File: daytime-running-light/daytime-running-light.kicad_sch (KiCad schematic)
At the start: 47 parts, among them J1 Conn_01x01_Socket, J2 Conn_01x01_Socket, J3 Conn_01x01_Socket, J4 Conn_01x02_Socket, Q1 2N3904, Q2 2N3904, Q3 IRFZ44N, Q4 IRF9321, SW1 SW_SPST, SW2 SW_SPST, U1 L7812, U2 4069, U3 4001

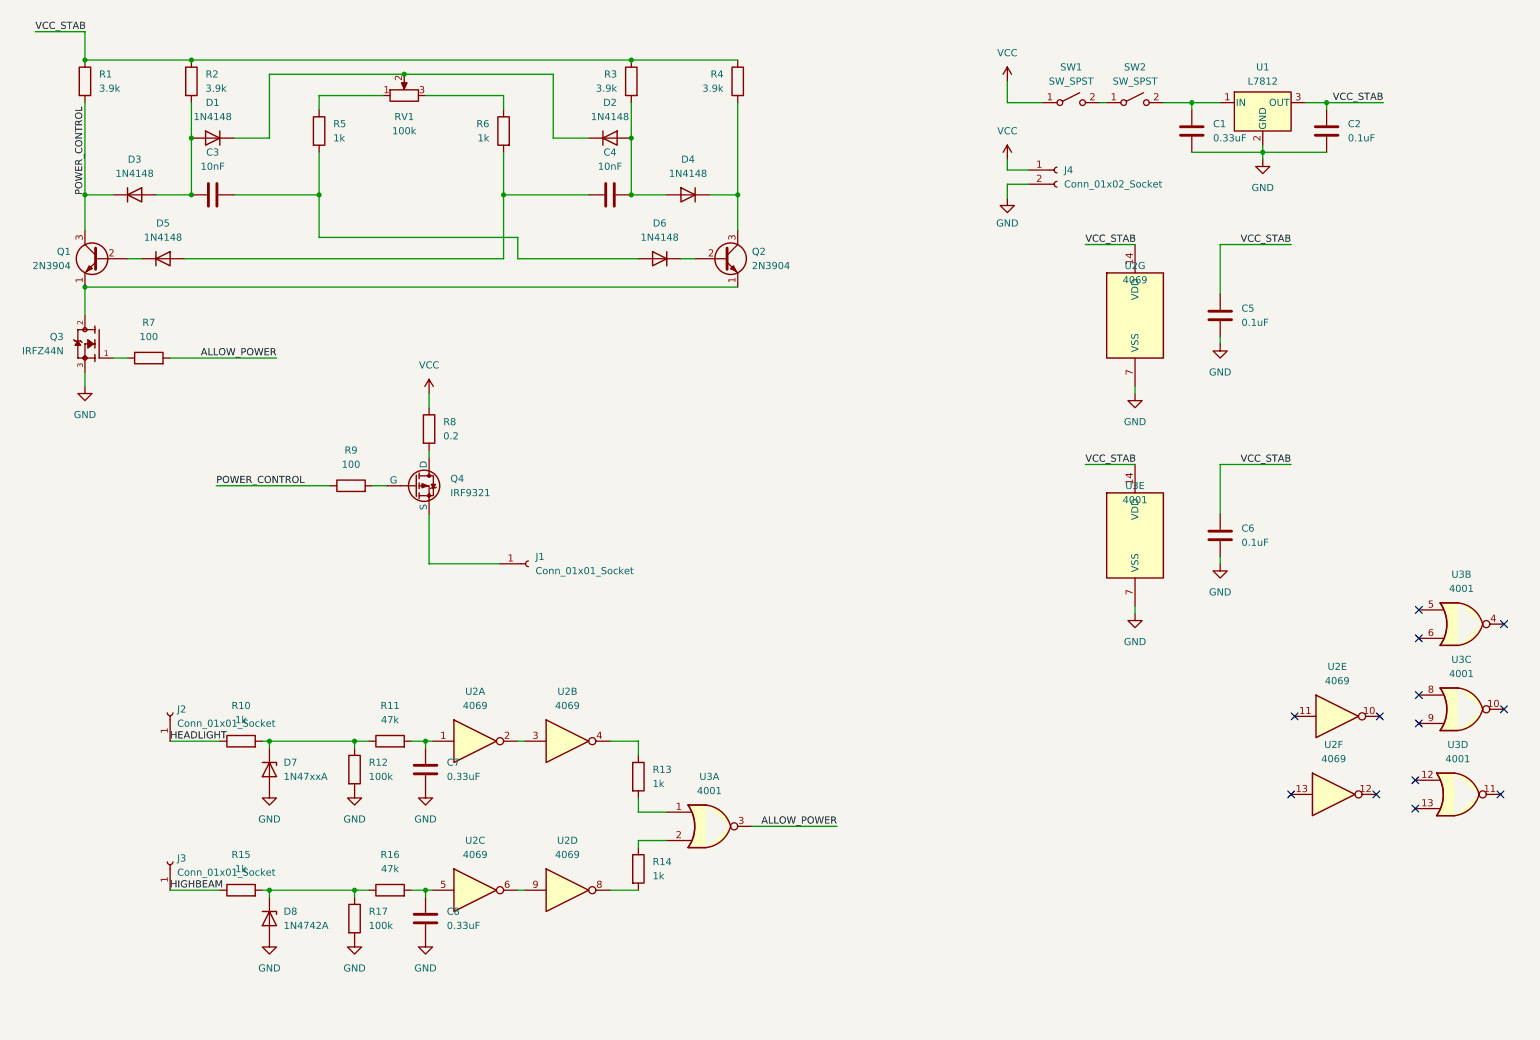
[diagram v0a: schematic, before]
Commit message: [drl] Change daytime running light to use TLC555 timer.
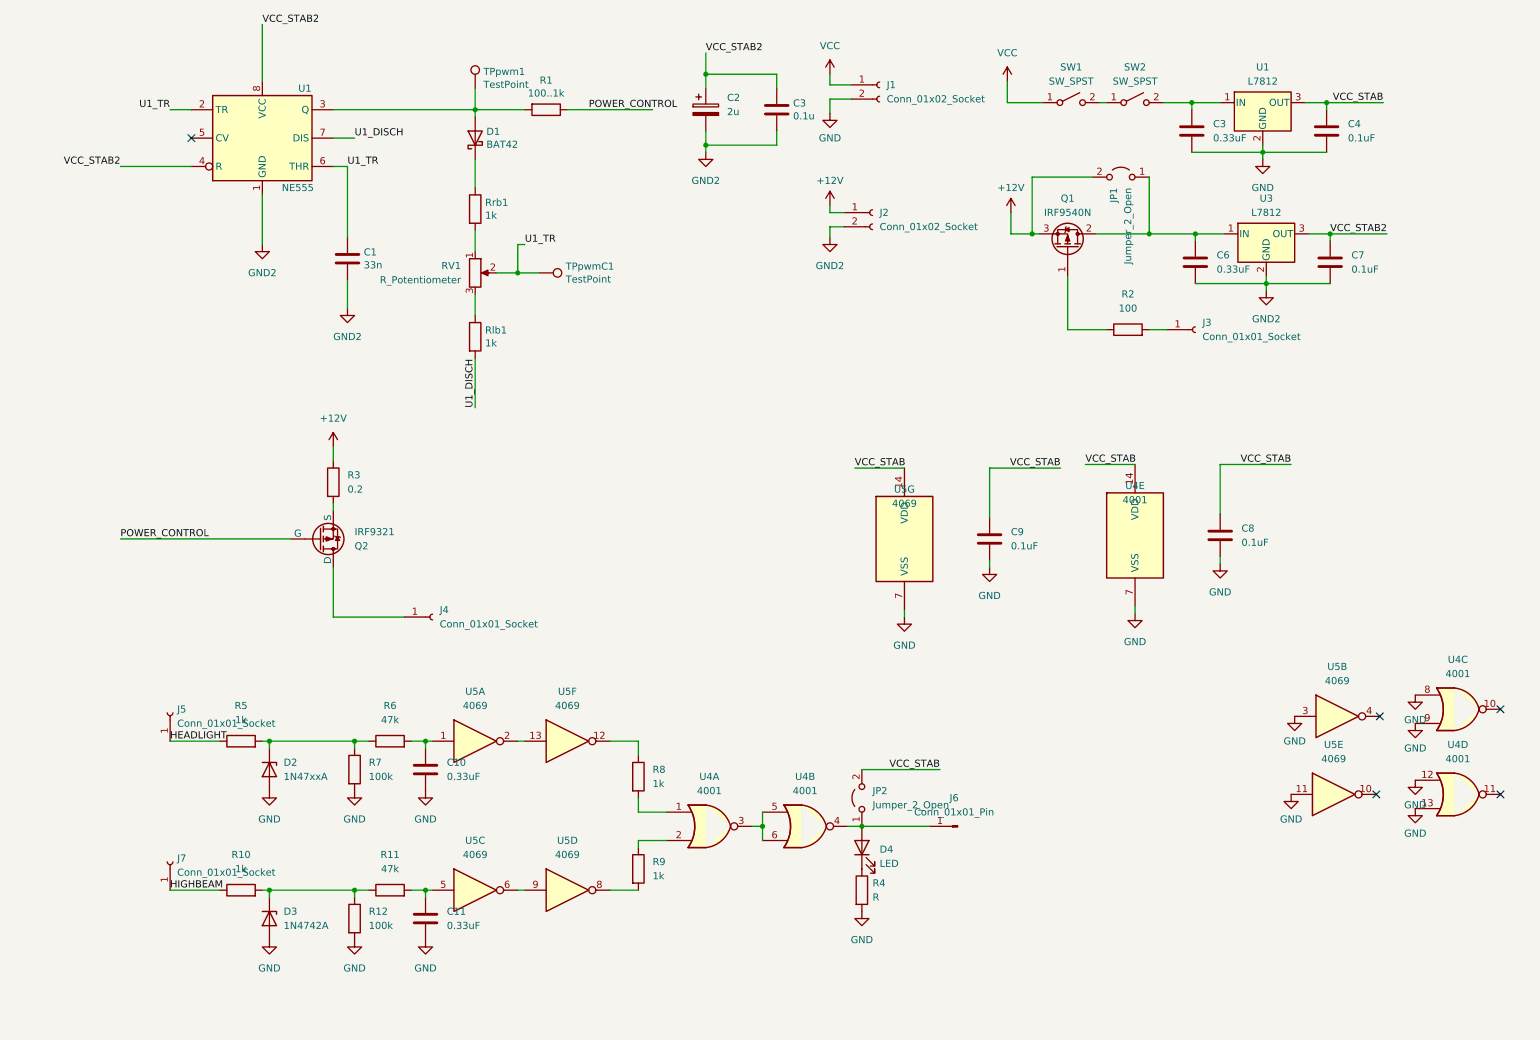
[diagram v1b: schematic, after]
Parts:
- removed C4: 10nF, Capacitor_THT:C_Disc_D6.0mm_W2.5mm_P5.00mm, symbol Device:C
- removed D1, D2, D3, D4, D5, D6: 1N4148, Diode_THT:D_DO-35_SOD27_P7.62mm_Horizontal, symbol Diode:1N4148
- removed Q1, Q2: 2N3904, Package_TO_SOT_THT:TO-92_Inline, symbol Transistor_BJT:2N3904
- removed Q3: IRFZ44N, Package_TO_SOT_THT:TO-220-3_Vertical, symbol IRFZ44N:IRFZ44N
- removed R2, R3: 3.9k, Resistor_THT:R_Axial_DIN0207_L6.3mm_D2.5mm_P7.62mm_Horizontal, symbol Device:R
- removed R5, R6: 1k, Resistor_THT:R_Axial_DIN0207_L6.3mm_D2.5mm_P2.54mm_Vertical, symbol Device:R
- removed R9: 100, Resistor_THT:R_Axial_DIN0207_L6.3mm_D2.5mm_P2.54mm_Vertical, symbol Device:R
- added C1: 33n, Capacitor_THT:C_Disc_D6.0mm_W2.5mm_P5.00mm, symbol Device:C
- added C2: 2u, Capacitor_THT:CP_Radial_D6.3mm_P2.50mm, symbol Device:C_Polarized
- added C6: 0.33uF, Capacitor_THT:C_Disc_D6.0mm_W2.5mm_P5.00mm, symbol Device:C
- added C7: 0.1uF, Capacitor_THT:C_Disc_D6.0mm_W2.5mm_P5.00mm, symbol Device:C
- added D1: BAT42, Diode_THT:D_DO-35_SOD27_P7.62mm_Horizontal, symbol Diode:BAT42
- added D4: LED, Connector_Wire:SolderWire-0.5sqmm_1x02_P4.6mm_D0.9mm_OD2.1mm, symbol Device:LED
- added J2: Conn_01x02_Socket, Connector_Wire:SolderWire-2.5sqmm_1x02_P8.8mm_D2.4mm_OD4.4mm, symbol Connector:Conn_01x02_Socket
- added J3: Conn_01x01_Socket, Connector_Wire:SolderWire-1.5sqmm_1x01_D1.7mm_OD3mm, symbol Connector:Conn_01x01_Socket
- added J6: Conn_01x01_Pin, Connector_Wire:SolderWire-1.5sqmm_1x01_D1.7mm_OD3mm, symbol Connector:Conn_01x01_Pin
- added JP1, JP2: Jumper_2_Open, Connector_Wire:SolderWire-0.75sqmm_1x02_P4.8mm_D1.25mm_OD2.3mm, symbol Jumper:Jumper_2_Open
- added Q1: IRF9540N, Package_TO_SOT_THT:TO-220-3_Vertical, symbol Transistor_FET:IRF9540N
- added Rlb1, Rrb1: 1k, Resistor_THT:R_Axial_DIN0207_L6.3mm_D2.5mm_P2.54mm_Vertical, symbol Device:R
- added TPpwm1, TPpwmC1: TestPoint, TestPoint:TestPoint_Pad_4.0x4.0mm, symbol Connector:TestPoint
- added U1: NE555, Package_DIP:DIP-8_W7.62mm, symbol smoke-machine-rescue:NE555-Timer
- added U3: L7812, Package_TO_SOT_THT:TO-220-3_Vertical, symbol Regulator_Linear:L7812
- C3: value 10nF -> 0.1u
- J1: renamed from J4; footprint Connector_Wire:SolderWire-2.5sqmm_1x02_P8.8mm_D2.4mm_OD4.4mm_Relief -> Connector_Wire:SolderWire-2.5sqmm_1x02_P8.8mm_D2.4mm_OD4.4mm
- J4: renamed from J1; footprint Connector_Wire:SolderWire-2.5sqmm_1x01_D2.4mm_OD3.6mm_Relief -> Connector_Wire:SolderWire-2.5sqmm_1x01_D2.4mm_OD3.6mm
- J5: renamed from J2; footprint Connector_Wire:SolderWire-1.5sqmm_1x01_D1.7mm_OD3mm_Relief -> Connector_Wire:SolderWire-1.5sqmm_1x01_D1.7mm_OD3mm
- J7: renamed from J3; footprint Connector_Wire:SolderWire-1.5sqmm_1x01_D1.7mm_OD3mm_Relief -> Connector_Wire:SolderWire-1.5sqmm_1x01_D1.7mm_OD3mm
- R1: value 3.9k -> 100..1k
- R3: renamed from R8; footprint Connector_Wire:SolderWire-1sqmm_1x02_P5.4mm_D1.4mm_OD2.7mm_Relief -> Connector_Wire:SolderWire-1sqmm_1x02_P5.4mm_D1.4mm_OD2.7mm
- R4: value 3.9k -> R
- RV1: value 100k -> R_Potentiometer; footprint Connector_Wire:SolderWire-1.5sqmm_1x03_P6mm_D1.7mm_OD3mm_Relief -> Connector_Wire:SolderWire-0.1sqmm_1x03_P3.6mm_D0.4mm_OD1mm_Relief
- SW1, SW2: footprint Connector_Wire:SolderWire-1.5sqmm_1x02_P6mm_D1.7mm_OD3mm_Relief -> Connector_Wire:SolderWire-2.5sqmm_1x02_P8.8mm_D2.4mm_OD4.4mm
- U1: footprint Package_TO_SOT_THT:TO-220-3_Horizontal_TabUp -> Package_TO_SOT_THT:TO-220-3_Vertical
- renumbered C7 to C10, C8 to C11, C1 to C3, C2 to C4, C6 to C8, C5 to C9, D7 to D2, D8 to D3, Q4 to Q2, R15 to R10, R16 to R11, R17 to R12, R7 to R2, R10 to R5, R11 to R6, R12 to R7, R13 to R8, R14 to R9, U3 to U4, U2 to U5
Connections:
- net GND: now also R4.2, U4.12, U4.13, U4.8, U4.9, U5.11, U5.3
- net POWER_CONTROL: now also Q2.2 (G), R1.1; no longer R1.2
- net VCC: no longer R3.1
- net VCC_STAB: now also JP2.2 (B); no longer R1.1, R4.1
- net GND2: now reaches C3.2
- net GND2: now also C1.2, C2.2, C6.2, C7.2, J2.2 (Pin_2), U1.1 (GND), U3.2 (GND)
- net at RV1.1: now also Rrb1.2
- net at R3.2: now also Q2.3 (S); no longer Q2.1 (D)
- net VCC_STAB2: now reaches C3.1
- net VCC_STAB2: now also C2.1, C7.1, U1.4 (R), U1.8 (VCC), U3.3 (OUT)
- net U1_TR: now reaches RV1.2
- net U1_TR: now also C1.1, TPpwmC1.1, U1.2 (TR), U1.6 (THR)
- net at R2.1: now also Q1.1 (G)
- net at R8.1: now also U5.12; no longer U5.4
- net at RV1.3: now also Rlb1.1
- net at U5.2: now also U5.13; no longer U5.3
- net at J4.1 (Pin_1): now also Q2.1 (D); no longer Q2.3 (S)
- net ALLOW_POWER: no longer names the net of R2.2
- net ALLOW_POWER: now also J3.1 (Pin_1); no longer U4.3
- new net: D1.2 (A), R1.2, TPpwm1.1, U1.3 (Q)
- new net: C6.1, JP1.1 (A), Q1.2 (D), U3.1 (IN)
- new net: U4.3, U4.5, U4.6
- new net: D4.1 (K), R4.1
- new net: D1.1 (K), Rrb1.1
- new net: D4.2 (A), J6.1 (Pin_1), JP2.1 (A), U4.4
- new net +12V: J2.1 (Pin_1), JP1.2 (B), Q1.3 (S), R3.1
- new net U1_DISCH: Rlb1.2, U1.7 (DIS)
- no-connect marks 13 -> 5
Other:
- moved on the sheet: C9, J1, J4, Q2, R2, R3, U4B, U4C, U4D, U5G

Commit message: [drl] Change schematic and PCB
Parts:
- removed U1: NE555, Package_DIP:DIP-8_W7.62mm, symbol smoke-machine-rescue:NE555-Timer
- added D5: 1.5KExxA, Diode_THT:D_DO-201AE_P15.24mm_Horizontal, symbol Diode:1.5KExxA
- added D6: 1N4148, Diode_THT:D_DO-35_SOD27_P7.62mm_Horizontal, symbol Diode:1N4148
- added Q3, Q4: BC548, LIB:TO-92_HandSolder2, symbol Transistor_BJT:BC548
- added Q5: BC548, Package_TO_SOT_THT:TO-92_HandSolder, symbol Transistor_BJT:BC548
- added R13, R16: 100, Resistor_THT:R_Axial_DIN0207_L6.3mm_D2.5mm_P2.54mm_Vertical, symbol Device:R
- added R14, R15: 10k..100k, Resistor_THT:R_Axial_DIN0207_L6.3mm_D2.5mm_P2.54mm_Vertical, symbol Device:R
- added R17: 10k, Resistor_THT:R_Axial_DIN0207_L6.3mm_D2.5mm_P2.54mm_Vertical, symbol Device:R
- added U2: TLC555xP, Package_DIP:DIP-8_W7.62mm, symbol Timer:TLC555xP
- C2: value 2u -> 0.1u
- Q1, U3: footprint Package_TO_SOT_THT:TO-220-3_Vertical -> LIB:TO-220-3_Vertical-mod
- R1: value 100..1k -> 10k
- R2: value 100 -> 10k
- RV1: value R_Potentiometer -> 51k
- Rlb1: value 1k -> 51k
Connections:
- net +12V: now also R15.1
- net GND2: now also Q3.3 (E), Q4.3 (E), U2.1 (GND)
- net POWER_CONTROL: now also D1.2 (A), R1.2, TPpwm1.1, U2.3 (Q); no longer Q2.2 (G), R1.1
- net U1_DISCH: now also U2.7 (DIS)
- net U1_TR: now also U2.2 (TR), U2.6 (THR)
- net VCC_STAB2: now also R14.1, U2.8 (VCC)
- net ALLOW_POWER_ON: now reaches Q1.1 (G), R2.1
- net ALLOW_POWER_ON: now also Q3.2 (B)
- net at Q2.3 (S), R3.2: now also D5.1 (A1), Q5.1 (C), R17.2
- net at J4.1 (Pin_1), Q2.1 (D): now also D5.2 (A2)
- net at D4.2 (A), JP2.1 (A), U4.4: now also R13.1; no longer J6.1 (Pin_1)
- new net: D6.1 (K), Q5.2 (B), R16.2, R17.1
- new net: Q4.2 (B), R1.1
- new net: Q3.1 (C), R14.2, U2.4 (R)
- new net: J6.1 (Pin_1), R13.2
- new net: D6.2 (A), Q2.2 (G), Q5.3 (E)
- new net POWER_CONTROL_INV: Q4.1 (C), R15.2, R16.1
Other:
- moved on the sheet: C10, C11, C8, C9, D2, D3, D4, J3, J4, J5, J6, J7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

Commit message: [drl] Change schematic and PCB
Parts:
- added R18: R, Resistor_THT:R_Axial_DIN0207_L6.3mm_D2.5mm_P2.54mm_Vertical, symbol Device:R
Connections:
- net GND: now also R18.2; no longer R4.2
- net VCC_STAB: now also R4.2; no longer JP2.2 (B)
- net at D4.2 (A), R13.1, U4.4: now also JP2.2 (B); no longer JP2.1 (A)
- new net: JP2.1 (A), R18.1
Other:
- moved on the sheet: D4, JP2, R4
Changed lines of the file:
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@@
     (stroke (width 0) (type default))
   )
-  (wire (pts (xy 137.795 159.385) (xy 150.495 159.385))
+  (wire (pts (xy 137.795 154.305) (xy 150.495 154.305))
     (stroke (width 0) (type default))
   )
@@
     (stroke (width 0) (type default))
   )
-  (wire (pts (xy 137.795 159.385) (xy 137.795 160.655))
+  (wire (pts (xy 137.795 154.305) (xy 137.795 155.575))
     (stroke (width 0) (type default))
   )
@@
     (effects (font (size 1.27 1.27)) (justify right bottom))
   )
-  (label "VCC_STAB" (at 150.495 159.385 180) (fields_autoplaced)
+  (label "VCC_STAB" (at 150.495 154.305 180) (fields_autoplaced)
     (effects (font (size 1.27 1.27)) (justify right bottom))
   )
@@
     )
   )
+  (symbol (lib_id "Device:R") (at 137.795 184.785 0) (unit 1)
+    (in_bom yes) (on_board yes) (dnp no) (fields_autoplaced)
+    (property "Reference" "R18" (at 139.7 183.515 0)
+      (effects (font (size 1.27 1.27)) (justify left))
+    )
+    (property "Value" "R" (at 139.7 186.055 0)
+      (effects (font (size 1.27 1.27)) (justify left))
+    )
+    (property "Footprint" "Resistor_THT:R_Axial_DIN0207_L6.3mm_D2.5mm_P2.54mm_Vertical" (at 136.017 184.785 90)
+      (effects (font (size 1.27 1.27)) hide)
+    )
+    (property "Datasheet" "~" (at 137.795 184.785 0)
+      (effects (font (size 1.27 1.27)) hide)
+    )
+    (pin "1")
+    (pin "2")
+    (instances
+      (project "daytime-running-light"
+        (path "/f8c2c6dd-d5ef-40d1-be2c-9a93444b1d43"
+          (reference "R18") (unit 1)
+        )
+      )
+    )
+  )
   (symbol (lib_id "power:GND") (at 157.48 33.655 0) (unit 1)
     (in_bom yes) (on_board yes) (dnp no) (fields_autoplaced)
@@
     )
   )
+  (symbol (lib_id "power:GND") (at 137.795 188.595 0) (unit 1)
+    (in_bom yes) (on_board yes) (dnp no) (fields_autoplaced)
+    (property "Reference" "#PWR025" (at 137.795 194.945 0)
+      (effects (font (size 1.27 1.27)) hide)
+    )
+    (property "Value" "GND" (at 137.795 193.675 0)
+      (effects (font (size 1.27 1.27)))
+    )
+    (property "Footprint" "" (at 137.795 188.595 0)
+      (effects (font (size 1.27 1.27)) hide)
+    )
+    (property "Datasheet" "" (at 137.795 188.595 0)
+      (effects (font (size 1.27 1.27)) hide)
+    )
+    (pin "1")
+    (instances
+      (project "daytime-running-light"
+        (path "/f8c2c6dd-d5ef-40d1-be2c-9a93444b1d43"
+          (reference "#PWR025") (unit 1)
+        )
+      )
+    )
+  )
   (symbol (lib_id "power:GND") (at 31.75 164.465 0) (unit 1)
     (in_bom yes) (on_board yes) (dnp no) (fields_autoplaced)
@@
     )
   )
-  (symbol (lib_id "Device:R") (at 137.795 182.245 0) (unit 1)
-    (in_bom yes) (on_board yes) (dnp no) (fields_autoplaced)
-    (property "Reference" "R4" (at 139.7 180.975 0)
-      (effects (font (size 1.27 1.27)) (justify left))
-    )
-    (property "Value" "R" (at 139.7 183.515 0)
-      (effects (font (size 1.27 1.27)) (justify left))
-    )
-    (property "Footprint" "Resistor_THT:R_Axial_DIN0207_L6.3mm_D2.5mm_P2.54mm_Vertical" (at 136.017 182.245 90)
-      (effects (font (size 1.27 1.27)) hide)
-    )
-    (property "Datasheet" "~" (at 137.795 182.245 0)
+  (symbol (lib_id "Device:R") (at 137.795 159.385 180) (unit 1)
+    (in_bom yes) (on_board yes) (dnp no) (fields_autoplaced)
+    (property "Reference" "R4" (at 135.89 160.655 0)
+      (effects (font (size 1.27 1.27)) (justify left))
+    )
+    (property "Value" "R" (at 135.89 158.115 0)
+      (effects (font (size 1.27 1.27)) (justify left))
+    )
+    (property "Footprint" "Resistor_THT:R_Axial_DIN0207_L6.3mm_D2.5mm_P2.54mm_Vertical" (at 139.573 159.385 90)
+      (effects (font (size 1.27 1.27)) hide)
+    )
+    (property "Datasheet" "~" (at 137.795 159.385 0)
       (effects (font (size 1.27 1.27)) hide)
     )
@@
     )
   )
-  (symbol (lib_id "power:GND") (at 137.795 186.055 0) (unit 1)
-    (in_bom yes) (on_board yes) (dnp no) (fields_autoplaced)
-    (property "Reference" "#PWR025" (at 137.795 192.405 0)
-      (effects (font (size 1.27 1.27)) hide)
-    )
-    (property "Value" "GND" (at 137.795 191.135 0)
-      (effects (font (size 1.27 1.27)))
-    )
-    (property "Footprint" "" (at 137.795 186.055 0)
-      (effects (font (size 1.27 1.27)) hide)
-    )
-    (property "Datasheet" "" (at 137.795 186.055 0)
-      (effects (font (size 1.27 1.27)) hide)
-    )
-    (pin "1")
-    (instances
-      (project "daytime-running-light"
-        (path "/f8c2c6dd-d5ef-40d1-be2c-9a93444b1d43"
-          (reference "#PWR025") (unit 1)
-        )
-      )
-    )
-  )
   (symbol (lib_id "Device:C_Polarized") (at 135.255 33.02 0) (unit 1)
     (in_bom yes) (on_board yes) (dnp no) (fields_autoplaced)
@@
     )
   )
-  (symbol (lib_id "Device:LED") (at 137.795 174.625 90) (unit 1)
-    (in_bom yes) (on_board yes) (dnp no) (fields_autoplaced)
-    (property "Reference" "D4" (at 140.97 174.9425 90)
+  (symbol (lib_id "Device:LED") (at 137.795 167.005 270) (unit 1)
+    (in_bom yes) (on_board yes) (dnp no) (fields_autoplaced)
+    (property "Reference" "D4" (at 134.62 166.6875 90)
       (effects (font (size 1.27 1.27)) (justify right))
     )
-    (property "Value" "LED" (at 140.97 177.4825 90)
+    (property "Value" "LED" (at 134.62 164.1475 90)
       (effects (font (size 1.27 1.27)) (justify right))
     )
-    (property "Footprint" "Connector_Wire:SolderWire-0.5sqmm_1x02_P4.6mm_D0.9mm_OD2.1mm" (at 137.795 174.625 0)
-      (effects (font (size 1.27 1.27)) hide)
-    )
-    (property "Datasheet" "~" (at 137.795 174.625 0)
+    (property "Footprint" "Connector_Wire:SolderWire-0.5sqmm_1x02_P4.6mm_D0.9mm_OD2.1mm" (at 137.795 167.005 0)
+      (effects (font (size 1.27 1.27)) hide)
+    )
+    (property "Datasheet" "~" (at 137.795 167.005 0)
       (effects (font (size 1.27 1.27)) hide)
     )
@@
     )
   )
-  (symbol (lib_id "Jumper:Jumper_2_Open") (at 137.795 165.735 90) (unit 1)
+  (symbol (lib_id "Jumper:Jumper_2_Open") (at 137.795 175.895 90) (unit 1)
     (in_bom yes) (on_board yes) (dnp no)
-    (property "Reference" "JP2" (at 139.7 164.465 90)
+    (property "Reference" "JP2" (at 139.7 174.625 90)
       (effects (font (size 1.27 1.27)) (justify right))
     )
-    (property "Value" "Jumper_2_Open" (at 139.7 167.005 90)
+    (property "Value" "Jumper_2_Open" (at 139.7 177.165 90)
       (effects (font (size 1.27 1.27)) (justify right))
     )
-    (property "Footprint" "Connector_Wire:SolderWire-0.75sqmm_1x02_P4.8mm_D1.25mm_OD2.3mm" (at 137.795 165.735 0)
-      (effects (font (size 1.27 1.27)) hide)
-    )
-    (property "Datasheet" "~" (at 137.795 165.735 0)
-      (effects (font (size 1.27 1.27)) hide)
-    )
+    (property "Footprint" "Connector_Wire:SolderWire-0.75sqmm_1x02_P4.8mm_D1.25mm_OD2.3mm" (at 137.795 175.895 0)
+      (effects (font (size 1.27 1.27)) hide)
+    )
+    (property "Datasheet" "~" (at 137.795 175.895 0)
+      (effects (font (size 1.27 1.27)) hide)
+    )
